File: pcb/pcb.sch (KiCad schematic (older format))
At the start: 24 parts, among them J1 USB_B_Micro, J2 AVR ISP connector, J3 Display connector, J4 Conn_01x02_Male, SW1 SSSS811101, SW2 SW_DIP_x01, SW3 SW_DIP_x01, U1 ATmega328P-AU, U2 MCP73831-2-OT, U3 AP9101CK6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

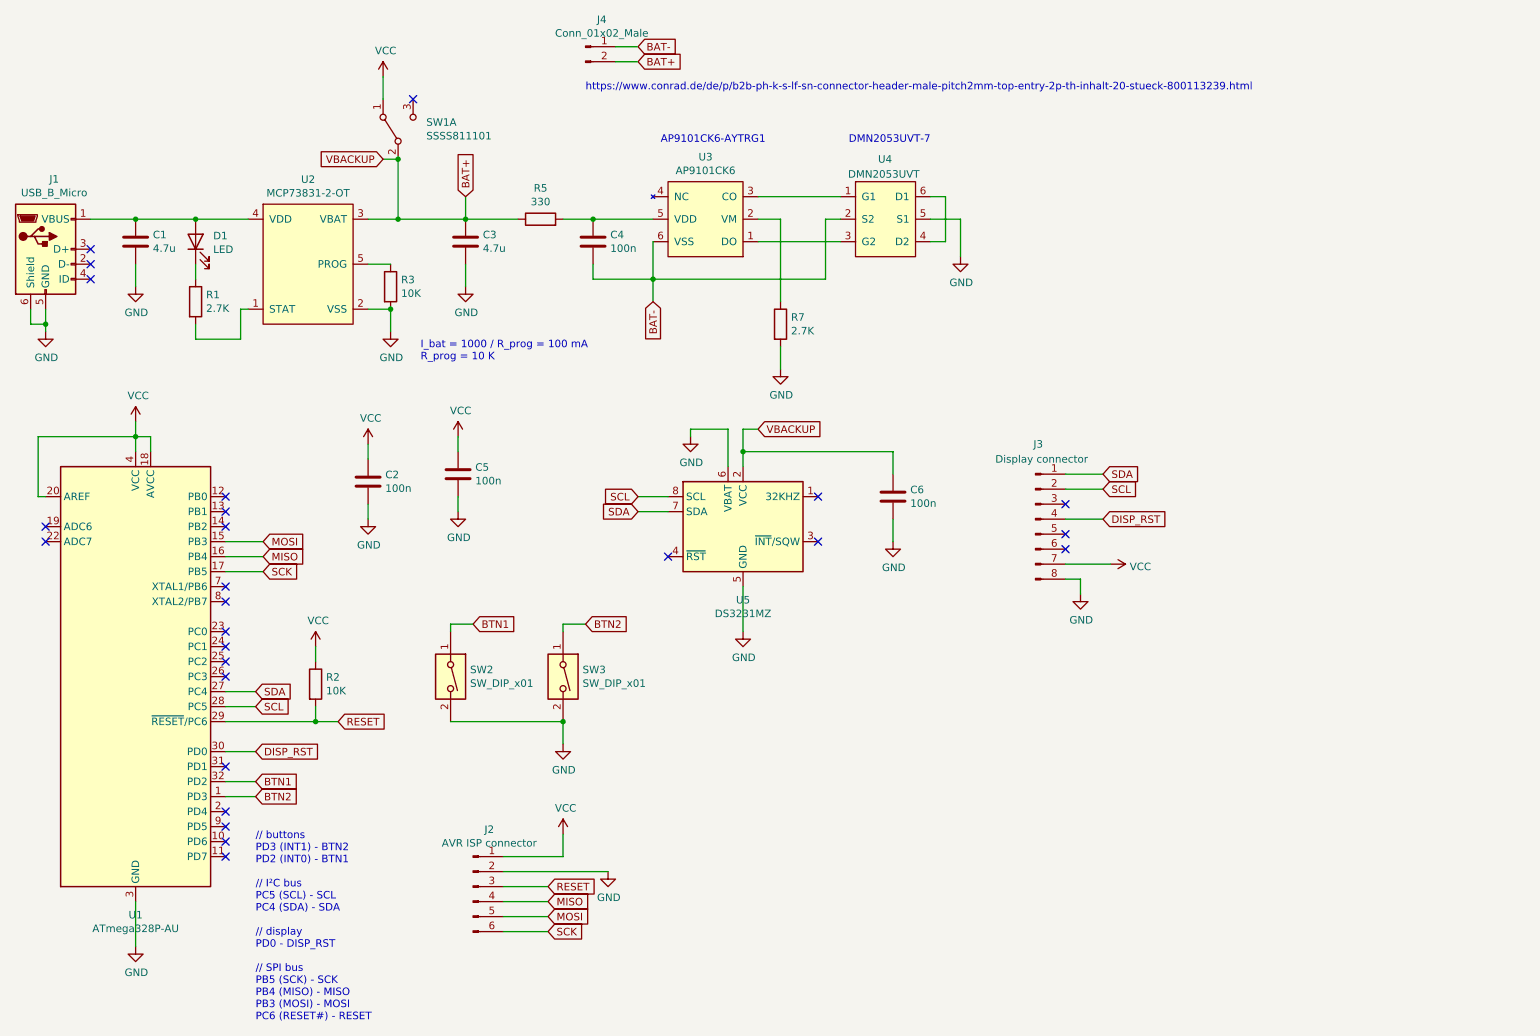
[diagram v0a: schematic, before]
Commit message: Added schematic to README
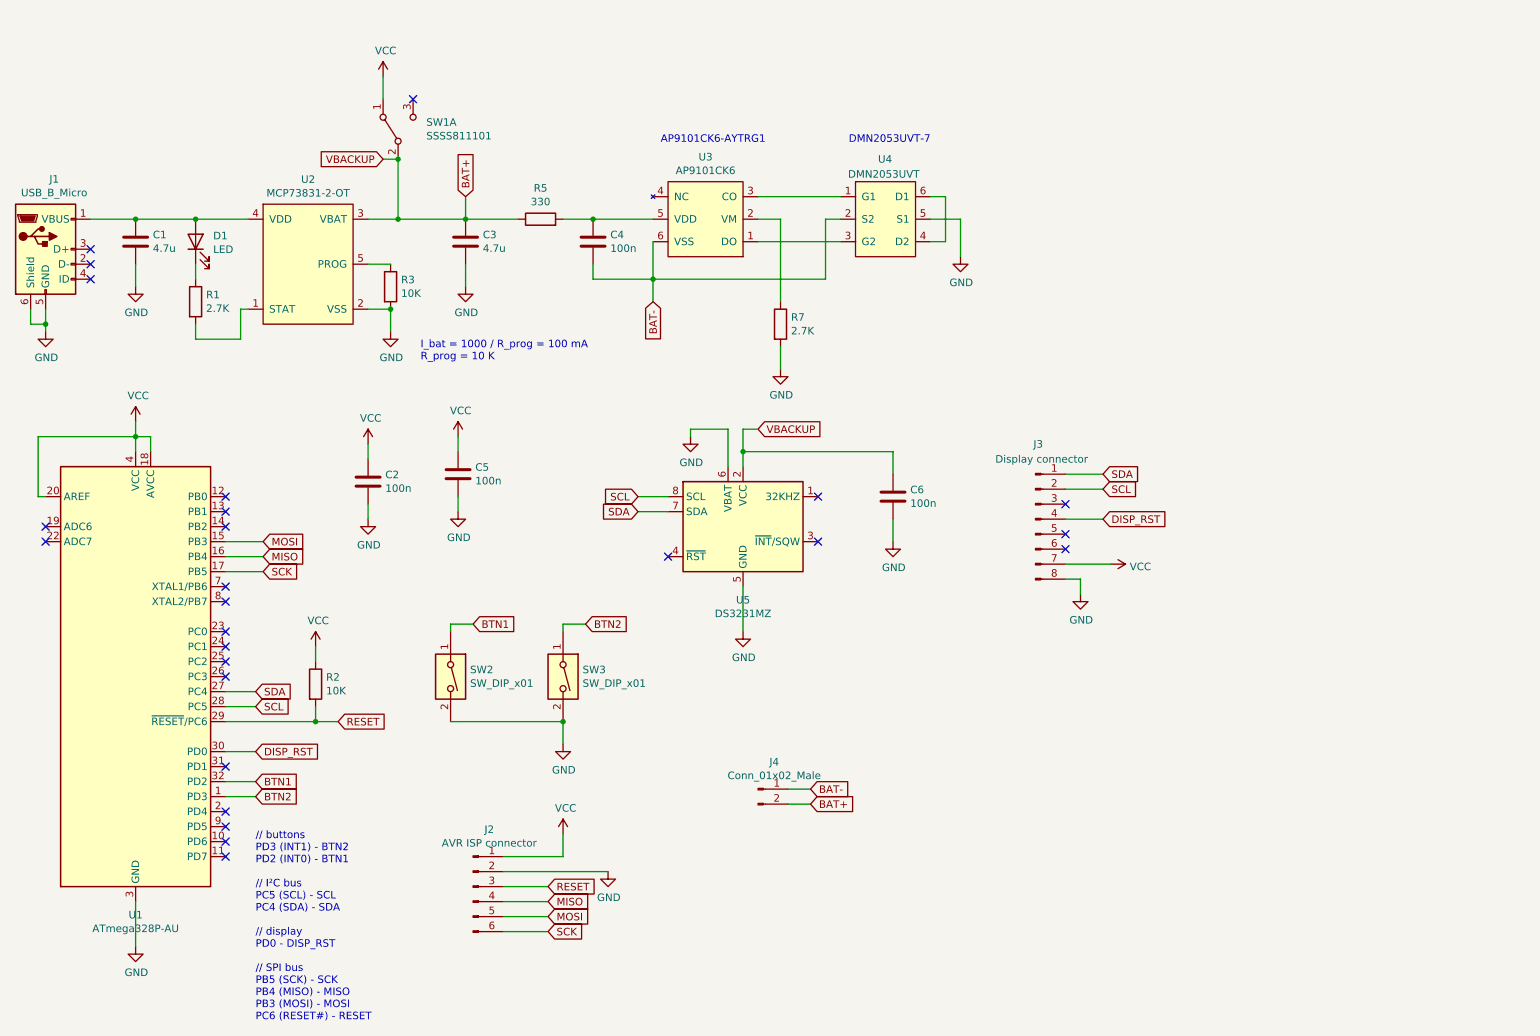
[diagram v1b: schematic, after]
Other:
- note removed: "https://www.conrad.de/de/p/b2b-ph-k-s-lf-sn-connector-header-male-pitch2mm-top-entry-2p-th-inhalt-20-stueck-800113239.html"
- moved on the sheet: J4
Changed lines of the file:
@@
 L Connector:Conn_01x02_Male J4
 U 1 1 5E792C70
-P 4800 900
-F 0 "J4" H 4908 1081 50  0000 C CNN
-F 1 "Conn_01x02_Male" H 4908 990 50  0000 C CNN
-F 2 "Connector_JST:JST_PH_B2B-PH-K_1x02_P2.00mm_Vertical" H 4800 900 50  0001 C CNN
-F 3 "~" H 4800 900 50  0001 C CNN
-	1    4800 900
+P 5950 5850
+F 0 "J4" H 6058 6031 50  0000 C CNN
+F 1 "Conn_01x02_Male" H 6058 5940 50  0000 C CNN
+F 2 "Connector_JST:JST_PH_B2B-PH-K_1x02_P2.00mm_Vertical" H 5950 5850 50  0001 C CNN
+F 3 "~" H 5950 5850 50  0001 C CNN
+	1    5950 5850
 	1    0    0    -1
 $EndComp
-Text GLabel 5150 1000 2    50   Input ~ 0
+Text GLabel 6300 5950 2    50   Input ~ 0
 BAT+
-Text GLabel 5150 900  2    50   Input ~ 0
+Text GLabel 6300 5850 2    50   Input ~ 0
 BAT-
 Wire Wire Line
-	5150 900  5000 900
+	6300 5850 6150 5850
 Wire Wire Line
-	5000 1000 5150 1000
+	6150 5950 6300 5950
 Wire Wire Line
 	5850 3600 6850 3600
@@
 Wire Wire Line
 	5850 3600 5850 3700
-Text Notes 4800 1200 0    50   ~ 0
-https://www.conrad.de/de/p/b2b-ph-k-s-lf-sn-connector-header-male-pitch2mm-top-entry-2p-th-inhalt-20-stueck-800113239.html
 $EndSCHEMATC
